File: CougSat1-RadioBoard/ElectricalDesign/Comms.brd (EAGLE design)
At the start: 90.4 x 95.8 mm, 409 parts, among them J1 700mm Antenna, J2 CougSat Card, J3 230mm Antenna, J4 SWD, Q1 DMN53D0LDW, Q2 DMN53D0LDW, Q3 DMN53D0LDW, Q4 CSD25402Q3A, Q5 CSD25402Q3A, U1 AD8515, U10 AD8515, U11 AD8515, U12 TXS0102DQM, U13 ADF4360, U14 MAAM-011229, U15 INA199C2, U16 AD8515, U17 AD8515, U18 LP5907MFX-3.1, U19 HMC545A, U2 AD8515, U20 INA199C1, U21 TPS61236, U22 AD8345, U23 AD9761, U24 TXS0102DQM, U25 TXS0102DQM, U26 TXS0102DQM, U27 MMZ09332B, U28 AD8515, U29 ADF4360, U3 AD7291, U30 TXS0102DQM, U31 INA199C2, U32 TXS0102DQM, U33 LP5907MFX-3.1, U34 MAAM-011229, U35 TXS0102DQM, U36 TXS0102DQM, U37 AD9761, U38 AD8346, U39 TXS0102DQM, U4 AD7291, U40 STM32L496VGT, U41 HMC452QS16G, U42 TXS0102DQM, U43 INA199C2, U44 ADF4360, U45 LP5907MFX-3.1, U46 IS25LP016D, U47 IS25LP016D, U48 GRF2133, U49 INA199C1, U5 MAAM-011229, U6 AD8348, U7 AD7291, U8 MAAM-011229, U9 TXS0102DQM, Y1 19.68MHz ±2.5ppm, Y2 19.68MHz ±2.5ppm, Y3 8MHz ±10ppm, Y4 32.768kHz ±10ppm, Y5 19.68MHz ±2.5ppm

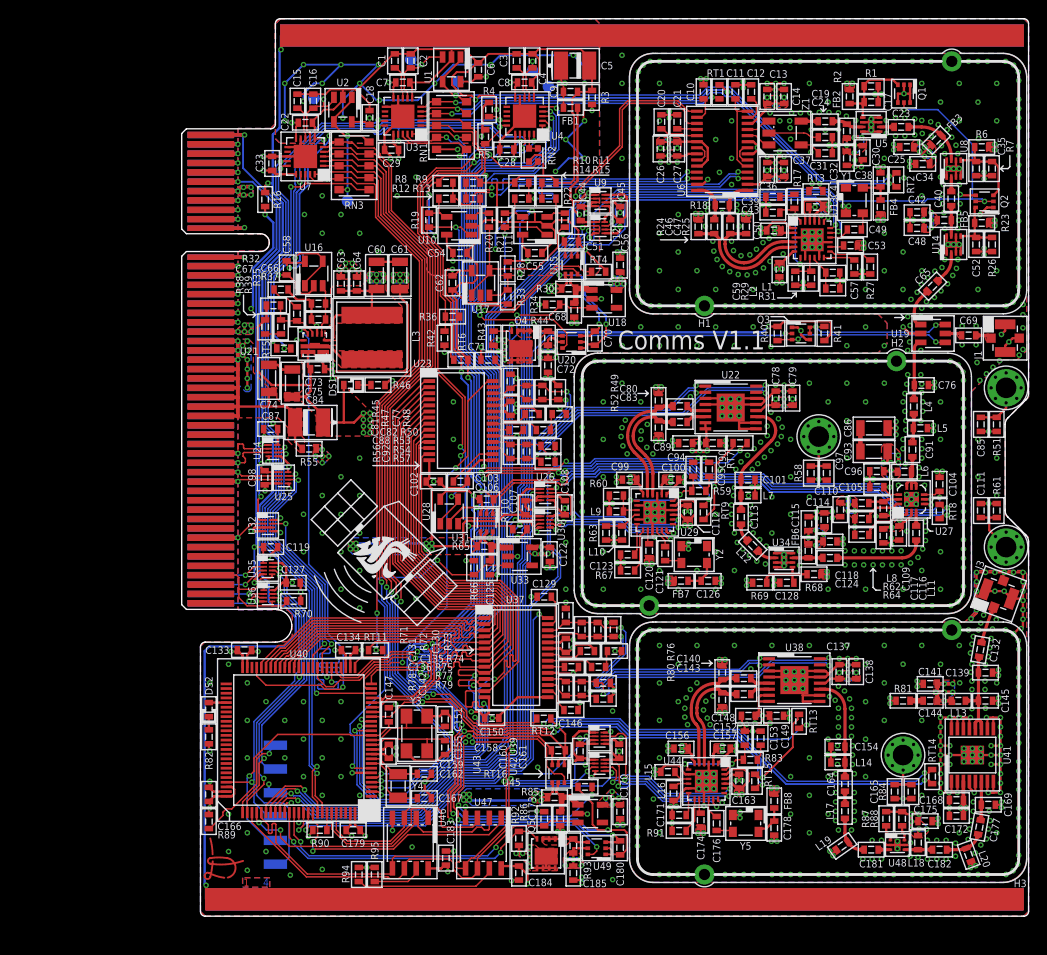
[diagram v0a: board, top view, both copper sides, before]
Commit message: Removed 230mm circuits
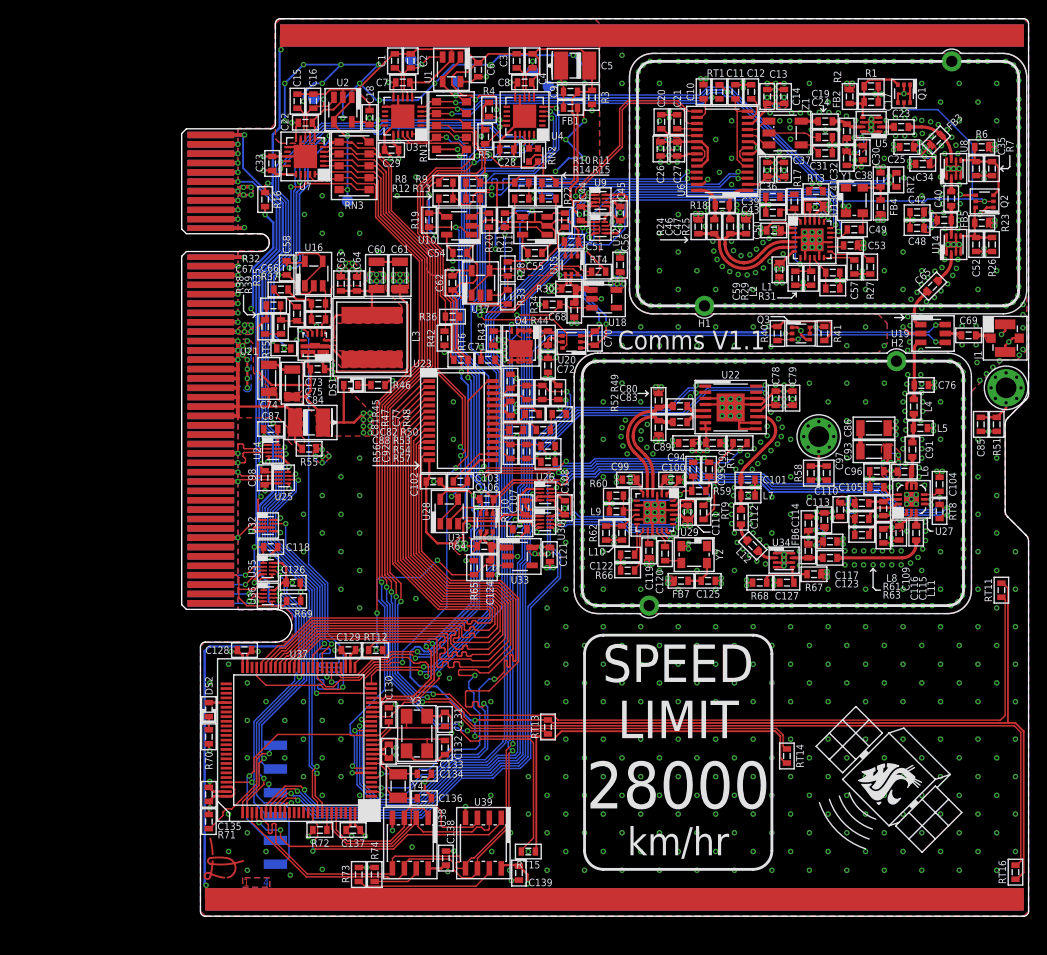
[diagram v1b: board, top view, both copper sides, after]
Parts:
- removed C140, C143, C176: 1nF 1%, CougsInSpace-Capacitors:1608
- removed C141, C170, C172, C173, C174, C185: 1µF 10%, CougsInSpace-Capacitors:1608
- removed C142: 560pF 1%, CougsInSpace-Capacitors:1608
- removed C144, C149, C168: 100pF 1%, CougsInSpace-Capacitors:1608
- removed C145: 2pF ±0.1pF, CougsInSpace-Capacitors:1608
- removed C146, C147, C150, C156, C157, C158, C159, C160, C161, C163, C165, C166, C175, C178, C179, C180, C183, C184: 100nF 10%, CougsInSpace-Capacitors:1608
- removed C148, C171: 10nF 10%, CougsInSpace-Capacitors:1608
- removed C151, C155: 8pF ±0.25, CougsInSpace-Capacitors:1608
- removed C152: 56pF 2%, CougsInSpace-Capacitors:1608
- removed C153: 270pF 1%, CougsInSpace-Capacitors:1608
- removed C154, C177: 10pF 5%, CougsInSpace-Capacitors:1608
- removed C162, C167: 15pF 1%, CougsInSpace-Capacitors:1608
- removed C164: 0.8pF ±0.1pF, CougsInSpace-Capacitors:1608
- removed C169: 4.7pF ±0.1, CougsInSpace-Capacitors:1608
- removed C181, C182: 33pF 5%, CougsInSpace-Capacitors:1608
- removed FB8: 1.5kΩ @ 100MHz, CougsInSpace-Coils:1608
- removed H5, H6, H7: M2, CougsInSpace-Hardware:MOUNTING_HOLE-2.2
- removed J4: SWD, CougsInSpace-Connectors:SMD2.54-1X06-R
- removed L13, L17, L20: 22nH 2%, CougsInSpace-Coils:1608
- removed L14, L15, L16: 1.6nH 5%, CougsInSpace-Coils:1608
- removed L18: 33nH 2%, CougsInSpace-Coils:1608
- removed L19: 18nH 2%, CougsInSpace-Coils:1608
- removed Q5: CSD25402Q3A, CougsInSpace-DiscreteSemi:SON-3333
- removed R75, R82, R89: 1kΩ 0.1%, CougsInSpace-Resistors:1608
- removed R76, R80: 49.9Ω 0.1%, CougsInSpace-Resistors:1608
- removed R77, R79: 1.33kΩ 0.1%, CougsInSpace-Resistors:1608
- removed R78: 1.74kΩ 0.1%, CougsInSpace-Resistors:1608
- removed R81: 5.6Ω 1%, CougsInSpace-Resistors:1608
- removed R83: 102kΩ 0.1%, CougsInSpace-Resistors:1608
- removed R84, R90: 0Ω <20mΩ, CougsInSpace-Resistors:1608
- removed R85, R93: 50mΩ 1%, CougsInSpace-Resistors:1608
- removed R86, R92, R94, R95: 10kΩ 0.1%, CougsInSpace-Resistors:1608
- removed R87, R91: 4.7kΩ 0.1%, CougsInSpace-Resistors:1608
- removed R88: 75Ω 0.1%, CougsInSpace-Resistors:1608
- removed U40: STM32L496VGT, CougsInSpace-IC-µController:QFP-100-1414
- removed U41: HMC452QS16G, CougsInSpace-RF:QSOP-16
- removed U42: TXS0102DQM, CougsInSpace-IC-Comms:X2SON-8
- removed U43: INA199C2, CougsInSpace-IC-Amplifiers:SOT363
- removed U44: ADF4360, CougsInSpace-RF:QFN-24-4040
- removed U45: LP5907MFX-3.1, CougsInSpace-IC-Power:SOT23-5
- removed U46, U47: IS25LP016D, CougsInSpace-IC-Memory:SO8
- removed U48: GRF2133, CougsInSpace-RF:DFN-6-1515
- removed U49: INA199C1, CougsInSpace-IC-Amplifiers:SOT363
- removed Y5: 19.68MHz ±2.5ppm, CougsInSpace-Clocks:SMD-3225
- C112: value 100nF 10% -> 2.4pF ±0.1pF
- C113: value 2.4pF ±0.1pF -> 100nF 10%
- C114: value 100nF 10% -> 47pF 5%
- C115: value 47pF 5% -> 100pF 1%
- C116: value 100pF 1% -> 1µF 10%
- C117, C120: value 1µF 10% -> 1nF 1%
- C118, C128: value 1nF 1% -> 100nF 10%
- C119: value 100nF 10% -> 1µF 10%
- C121, C124: value 1nF 1% -> 1µF 10%
- C122: value 1µF 10% -> 10nF 10%
- C123: value 10nF 10% -> 1nF 1%
- C125: value 1µF 10% -> 100nF 10%
- C127: value 100nF 10% -> 1nF 1%
- C130: value 560pF 1% -> 100nF 10%
- C131: value 100nF 10% -> 8pF ±0.25
- C132: value 100pF 1% -> 8pF ±0.25
- C134, C136: value 100nF 10% -> 15pF 1%
- C137: value 100pF 1% -> 100nF 10%
- C138: value 10nF 10% -> 100nF 10%
- C139: value 4.7pF ±0.1 -> 100nF 10%
- H3: value Can - 230mm -> M2; device CougsInSpace-Hardware:SHIELD-2641 -> CougsInSpace-Hardware:MOUNTING_HOLE-2.2
- J3: value 230mm Antenna -> SWD; device CougsInSpace-Connectors:U.FL -> CougsInSpace-Connectors:SMD2.54-1X06-R
- LOGO1: value SIGNATUREBRADLEY -> Satellite 16mm; device CougsInSpace-Aesthetics:SIGN-BRADLEY -> CougsInSpace-Aesthetics:CIS-SATELLITE-16
- LOGO2: value Satellite 16mm -> SIGNATUREBRADLEY; device CougsInSpace-Aesthetics:CIS-SATELLITE-16 -> CougsInSpace-Aesthetics:SIGN-BRADLEY
- R61: value 0Ω <20mΩ -> 2kΩ 0.1%
- R62: value 2kΩ 0.1% -> 470Ω 0.5%
- R63: value 470Ω 0.5% -> 1.74kΩ 0.1%
- R64: value 1.74kΩ 0.1% -> 50mΩ 1%
- R65: value 50mΩ 1% -> 10kΩ 0.1%
- R66: value 10kΩ 0.1% -> 4.7kΩ 0.1%
- R67: value 4.7kΩ 0.1% -> 2kΩ 0.1%
- R69: value 2kΩ 0.1% -> 1kΩ 0.1%
- R71: value 1.33kΩ 0.1% -> 1kΩ 0.1%
- R72: value 1.74kΩ 0.1% -> 0Ω <20mΩ
- R73: value 1.33kΩ 0.1% -> 10kΩ 0.1%
- R74: value 8.45kΩ 0.1% -> 10kΩ 0.1%
- U37: value AD9761 -> STM32L496VGT; device CougsInSpace-IC-Conversion:SSOP-28 -> CougsInSpace-IC-µController:QFP-100-1414
- U38: value AD8346 -> IS25LP016D; device CougsInSpace-RF:TSSOP-16 -> CougsInSpace-IC-Memory:SO8
- U39: value TXS0102DQM -> IS25LP016D; device CougsInSpace-IC-Comms:X2SON-8 -> CougsInSpace-IC-Memory:SO8
- moved J3 75.6 mm to (15.0, -36.0), flipped to the bottom, turned to 90 degrees
- moved LOGO1 71.5 mm to (75.5, -33.3)
- moved RT11 67.1 mm to (87.5, -13.1), turned to 90 degrees
- moved C118 59.7 mm to (9.50, -8.50)
- moved C128 58.3 mm to (6.70, -19.5), turned to 0 degrees
- moved C132 58.1 mm to (28.1, -29.9), turned to 270 degrees
- moved C137 54.6 mm to (18.3, -38.7), turned to 180 degrees
- moved C139 54.2 mm to (36.0, -43.3), turned to 270 degrees
- moved C127 52.7 mm to (64.6, -12.3), turned to 180 degrees
- moved R69 49.8 mm to (11.9, -14.2), turned to 180 degrees
- moved LOGO3 48.7 mm to (53.0, -29.9), flipped to the top
- moved C138 48.1 mm to (28.2, -41.7)
- moved RT16 46.8 mm to (89.0, -43.2), turned to 270 degrees
- moved U38 44.5 mm to (24.4, -40.1), turned to 270 degrees
- moved C126 44.3 mm to (11.9, -12.3)
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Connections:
- removed net !230_CS: U39.7, U44.19
- removed net !PC_5.0V-0: Q5.4, R92.1, U40.86
- removed net !RFCLK_CS-230: U39.2, U40.89
- removed net 230_MOSI: U42.6, U44.18
- removed net 230_SCK: U42.7, U44.17
- removed net 3.1V_0: C131.1, C135.1, C137.1, C138.1, C148.1, C149.1, C156.1, C157.1, C161.1, C163.1, C170.1, C174.1, FB8.2, R76.2, R80.2, U37.23, U38.12, U38.7, U38.8, U39.5, U39.8, U42.5, U42.8, U44.2, U44.21, U44.23, U44.6, U45.5
- removed net 5.0V_0: C141.1, C144.1, C168.1, C172.1, C175.1, C185.1, L13.2, L18.2, R87.2, R88.2, R93.1, U41.3, U49.5
- removed net ANTENNA_230_COAX: C132.2, J3.CENTER
- removed net CHASSIS_230-0: C111.1, H5.1, H5.V1, H5.V2, H5.V3, H5.V4, H5.V5, H5.V6, H5.V7, H5.V8, R61.2
- removed net CHASSIS_230-1: C165.1, H4.1, H4.V1, H4.V2, H4.V3, H4.V4, H4.V5, H4.V6, H4.V7, H4.V8, R84.2
- removed net DAC_BUS_CLK-230: U37.11, U37.12, U40.4
- removed net DAC_COMP1-230: C129.1, U37.27
- removed net DAC_COMP2-230: C135.2, U37.22
- removed net DAC_COMP3-230: C146.1, U37.16
- removed net DAC_FSADJ-230: R75.2, U37.21
- removed net DAC_FSASJ_MID-230: R74.2, R75.1
- removed net DAC_REFIO-230: C136.1, U37.20
- removed net DAC_SLEEP-230: U37.28, U40.88
- removed net I_3.1V-0: U4.2, U43.6
- removed net I_3.1V-0N: C173.1, R85.1, U43.5, U45.1
- removed net I_5.0V-0: U4.1, U49.6
- removed net I_5.0V-0P: Q5.1, Q5.2, Q5.3, R93.2, U49.4
- removed net MOD_230_ID_N: C130.2, R72.1, R73.2, U37.25, U38.2
- removed net MOD_230_ID_P: C130.1, R71.2, R72.2, U37.26, U38.1
- removed net MOD_230_LOI_N: C140.2, U38.5
- removed net MOD_230_LOI_P: C143.2, U38.6
- removed net MOD_230_QD_N: C142.2, R77.2, R78.1, U37.18, U38.15
- removed net MOD_230_QD_P: C142.1, R78.2, R79.2, U37.17, U38.16
- removed net MOD_230_RFOUT: C154.1, C164.1, L14.2, U38.11
- removed net MOD_LNA_230_EN: R87.1, U48.1
- removed net MOD_LNA_230_RFIN: C181.2, U48.3
- removed net MOD_LNA_230_RFINMID1: C164.2, L17.1
- removed net MOD_LNA_230_RFINMID2: C181.1, L17.2, L19.2
- removed net MOD_LNA_230_RFOUT: C182.1, L18.1, U48.4
- removed net MOD_LNA_230_VDD1: R88.1, U48.6
- removed net MOD_PA_230_RC: C144.2, R81.2
- removed net MOD_PA_230_RFIN: C169.1, C177.2, U41.6
- removed net MOD_PA_230_RFINMID: C177.1, C182.2, L20.2
- removed net MOD_PA_230_RFOUT: C132.1, C139.1, C145.1, L13.1, U41.11, U41.12
- removed net MUXOUT-230: U40.90, U44.20
- removed net PC_3.1V-0: R86.2, U40.87, U45.3
- removed net REF_CLK_VDD-0: C178.1, FB8.1, Y5.4
- removed net RFCLK_CC-230: C171.1, U44.12
- removed net RFCLK_CN-230: C174.2, U44.14
- removed net RFCLK_CP-230: C152.1, R83.2, U44.24, U44.7
- removed net RFCLK_L1-230: L15.2, U44.9
- removed net RFCLK_L2-230: L16.2, U44.10
- removed net RFCLK_OUT-230_N: C140.1, R76.1, U44.5
- removed net RFCLK_OUT-230_P: C143.1, R80.1, U44.4
- removed net RFCLK_REFIN-230: C176.2, U44.16
- removed net RFCLK_REFOUT-230: C176.1, Y5.3
- removed net RFCLK_RSET-230: R91.2, U44.13
- removed net RFCLK_VTUNE_FILTER-230: C153.1, R83.1
- removed net TEMP_CLK_230: RN3.8, RT15.1, U7.2
- removed net TEMP_DAC_230: RN3.7, RT12.1, U7.20
- removed net TEMP_LDO-0: RN3.3, RT16.1, U7.1
- removed net TEMP_MOD_230: RN3.9, RT13.1, U7.4
- removed net TEMP_PA_230: RN3.2, RT14.1, U7.3
- new net TEMP_PCB_0: RN3.7, RT13.1, U7.20
- new net TEMP_PCB_1: RN3.3, RT15.1, U7.1
- new net TEMP_PCB_2: RN3.8, RT14.1, U7.2
- new net TEMP_PCB_3: RN3.2, RT16.1, U7.3
- new net TEMP_PCB_4: RN3.9, RT11.1, U7.4
- net !ADC_RESET: now also U37.29; no longer U40.29
- net !COM_SPI_CS: now also U37.35; no longer U40.35
- net !FLASH_CS-A: now also U37.91, U39.1; no longer U40.91, U47.1
- net !FLASH_CS-B: now also U37.95, U38.1; no longer U40.95, U46.1
- net !FLASH_WP: now also U37.96, U38.3, U39.3; no longer U40.96, U46.3, U47.3
- net !NRST: now also C130.1, J3.5, U37.14; no longer C147.1, J4.5, U40.14
- net !PC_5.0V-1: now also U37.17; no longer U40.17
- net !RFCLK_CS-DEMOD: now also U37.18; no longer U40.18
- net !RFCLK_CS-MOD: now also U37.83; no longer U40.83
- net !RX_LNA_EN: now also U37.15; no longer U40.15
- net 3.1V_1: now also C111.1, C113.1, C117.1, C119.1, C121.1, R67.2; no longer C112.1, C115.1, C118.1, C120.1, C122.1, R68.2
- net 3.3V_5: now also C118.1; no longer C119.1
- net 3.3V_6: now also C126.1, C128.1, C129.1, C135.1, C137.1, C138.1, C139.1, R64.2, R71.2, R73.2, R74.2, U37.100, U37.11, U37.28, U37.50, U37.6, U37.73, U37.75, U38.8, U39.8; no longer C127.1, C134.1, C150.1, C159.1, C160.1, C166.1, C179.1, C183.1, C184.1, R65.2, R85.2, R89.2, R94.2, R95.2, U37.14, U39.1, U40.100, U40.11, U40.28, U40.50, U40.6, U40.73, U40.75, U42.1, U43.4, U46.8, U47.8
- net 5.0V: no longer Q5.5, Q5.6, Q5.7, Q5.8, Q5.PAD, R92.2
- net 5.0V_1: now also C115.1, R61.2, R63.2; no longer C117.1, R62.2, R64.2
- net AGND: now also U37.19, U37.20; no longer C158.2, C180.2, U40.19, U40.20, U43.1, U43.2, U49.1, U49.2
- net ANTENNA_SW: now also U37.82; no longer U40.82
- net AVDD: now also U37.21, U37.22; no longer C158.1, C180.1, U40.21, U40.22, U43.3, U49.3
- net BOOT0: now also R72.2, U37.94; no longer R90.2, U40.94
- net CHASSIS_700-0: now also H4.1, H4.V1, H4.V2, H4.V3, H4.V4, H4.V5, H4.V6, H4.V7, H4.V8; no longer H7.1, H7.V1, H7.V2, H7.V3, H7.V4, H7.V5, H7.V6, H7.V7, H7.V8
- net CHASSIS_700-1: now also H3.1, H3.V1, H3.V2, H3.V3, H3.V4, H3.V5, H3.V6, H3.V7, H3.V8; no longer H6.1, H6.V1, H6.V2, H6.V3, H6.V4, H6.V5, H6.V6, H6.V7, H6.V8
- net COM_SPI_MISO: now also U37.31; no longer U40.31
- net COM_SPI_MOSI: now also U37.32; no longer U40.32
- net COM_SPI_SCK: now also U37.23; no longer U40.23
- net CTRL_SYNC: now also U37.33; no longer U40.33
- net DAC_BUS_0: now also U37.5; no longer U37.10, U40.5
- net DAC_BUS_1: now also U37.38; no longer U37.9, U40.38
- net DAC_BUS_2: now also U37.39; no longer U37.8, U40.39
- net DAC_BUS_3: now also U37.40; no longer U37.7, U40.40
- net DAC_BUS_4: now also U37.41; no longer U37.6, U40.41
- net DAC_BUS_5: now also U37.42; no longer U37.5, U40.42
- net DAC_BUS_6: now also U37.43; no longer U37.4, U40.43
- net DAC_BUS_7: now also U37.44; no longer U37.3, U40.44
- net DAC_BUS_8: now also U37.45; no longer U37.2, U40.45
- net DAC_BUS_9: now also U37.46; no longer U37.1, U40.46
- net DAC_BUS_CLK-700: now also U37.3; no longer U40.3
- net DAC_SELECT_I/!Q: now also U37.2; no longer U37.13, U40.2
- net DAC_SLEEP-700: now also U37.34; no longer U40.34
- net DEMOD_ENABLE: now also U37.25; no longer U40.25
- net DEMOD_ID: now also U37.24; no longer U40.24
- net DEMOD_QD: now also U37.26; no longer U40.26
- net DEMOD_VGIN: now also U37.30; no longer U40.30
- net DGND: now also C113.2, C121.2, C124.2, C130.2, C132.2, C135.2, J3.3, R62.1, R65.1, R68.1, R72.1, U37.10, U37.27, U37.49, U37.74, U37.99; no longer C112.2, C119.2, C123.2, C141.2, C145.2, C146.2, C147.2, C148.2, C149.2, C150.2, C151.2, C152.2, C153.2, C154.2, C155.2, C156.2, C157.2, C159.2, C160.2, C161.2, C162.2, C163.2, C165.2, C166.2, C167.2, C168.2, C169.2, C170.2, C171.2, C172.2, C173.2, C175.2, C178.2, C179.2, C183.2, C184.2, C185.2, H3.1, H3.2, J3.SHIELD@1, J3.SHIELD@13, J3.SHIELD@2, J4.3, L14.1, L15.1, L16.1, L19.1, L20.1, R61.1, R63.1, R67.1, R71.1, R73.1, R74.1, R77.1, R79.1, R81.1, R82.1, R84.1, R86.1, R90.1, R91.1, U37.15, U37.19, U37.24, U38.10, U38.13, U38.14, U38.3, U38.9, U38.PAD, U39.3, U39.6, U40.10, U40.27, U40.49, U40.74, U40.99, U41.1, U41.10, U41.13, U41.14, U41.15, U41.16, U41.2, U41.4, U41.5, U41.7, U41.8, U41.9, U41.PAD, U42.4, U44.1, U44.11, U44.15, U44.22, U44.3, U44.8, U44.PAD, U45.2, U46.4, U47.4, U48.2, U48.5, U48.PAD, Y5.2
- net FLASH_HOLD-A: now also R73.1, U39.7; no longer R94.1, U47.7
- net FLASH_HOLD-B: now also R74.1, U38.7; no longer R95.1, U46.7
- net I2C_SCL: now also U37.92; no longer U40.92
- net I2C_SDA: now also U37.93; no longer U40.93
- net I_3.1V-1N: now also C124.1, R64.1; no longer C125.1, R65.1
- net JTAG_EN_COMMS: now also R69.2; no longer R70.2
- net JTAG_TCK: now also J3.2, U37.76; no longer J4.2, U40.76
- net JTAG_TDI: now also U37.77; no longer U40.77
- net JTAG_TDO: now also J3.6, U37.37; no longer J4.6, U40.37
- net JTAG_TMS: now also J3.4, U37.72; no longer J4.4, U40.72
- net LED_A: now also U37.55; no longer U40.55
- net LED_C: now also R70.2; no longer R82.2
- net MOD_700_RFOUT: now also C112.1; no longer C113.1
- net MOD_LNA_700_RFINMID: now also C112.2; no longer C113.2
- net MOD_LNA_700_RFOUT: now also C123.1; no longer C124.1
- net MOD_PA_700_RFINMID: now also C123.2; no longer C124.2
- net MUXOUT-DEMOD: now also U37.81; no longer U40.81
- net MUXOUT-MOD: now also U37.85; no longer U40.85
- net OSC32_IN: now also C136.1, U37.8; no longer C167.1, U40.8
- net OSC32_OUT: now also C134.1, U37.9; no longer C162.1, U40.9
- net OSC_IN: now also C132.1, U37.12; no longer C155.1, U40.12
- net OSC_OUT: now also C131.1, U37.13; no longer C151.1, U40.13
- net PA_PD-700: now also U37.84; no longer U40.84
- net PA_VBA1-700: now also R63.1; no longer R64.1
- net PA_VBA2-700: now also R61.1; no longer R62.1
- net PC_3.1V-1: now also R65.2, U37.7; no longer R66.2, U40.7
- net PC_3.1V-2: now also U37.16; no longer U40.16
- net PREAMP_700_BIAS: now also C127.1, R67.1, R68.2; no longer C128.1, R68.1, R69.2
- net REF_CLK_VDD-1: now also C125.1; no longer C126.1
- net REG_EN-5: now also U37.47; no longer U40.47
- net RFCLK_CC-MOD: now also C122.1; no longer C123.1
- net RFCLK_CN-MOD: now also C119.2; no longer C120.2
- net RFCLK_L2-MOD: now also R62.2; no longer R63.2
- net RFCLK_REFIN-MOD: now also C120.2; no longer C121.2
- net RFCLK_REFOUT-MOD: now also C120.1; no longer C121.1
- net RFCLK_RSET-MOD: now also R66.2; no longer R67.2
- net SPI_MISO: now also U37.79, U38.2, U39.2; no longer U40.79, U46.2, U47.2
- net SPI_MOSI: now also U37.80, U38.5, U39.5; no longer U40.80, U42.3, U46.5, U47.5
- net SPI_SCK: now also U37.78, U38.6, U39.6; no longer U40.78, U42.2, U46.6, U47.6
- net SWD_VSENSE: now also J3.1, R71.1; no longer J4.1, R89.1
- net TEMP_COMMS: now also RT12.1; no longer RT11.1
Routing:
- net TEMP_PCB_3: track 0.00 -> 149.6 mm, vias 0 -> 2
- net TEMP_PCB_4: track 0.00 -> 146.4 mm, vias 0 -> 2
- net TEMP_PA_230: track 129.1 -> 0.00 mm, vias 4 -> 0
- net 3.1V_0: track 127.6 -> 0.00 mm, vias 31 -> 0
- net TEMP_MOD_230: track 115.5 -> 0.00 mm, vias 4 -> 0
- net TEMP_CLK_230: track 112.2 -> 0.00 mm, vias 4 -> 0
- net TEMP_PCB_2: track 0.00 -> 111.0 mm, vias 0 -> 2
- net I_5.0V-0: track 108.5 -> 0.00 mm, vias 4 -> 0
- net TEMP_LDO-0: track 98.8 -> 0.00 mm, vias 4 -> 0
- net I_3.1V-0: track 95.9 -> 0.00 mm, vias 2 -> 0
- net TEMP_PCB_1: track 0.00 -> 95.1 mm, vias 0 -> 2
- net TEMP_DAC_230: track 87.5 -> 0.00 mm, vias 2 -> 0
- net 5.0V_0: track 86.0 -> 0.00 mm, vias 19 -> 0
- net TEMP_PCB_0: track 0.00 -> 84.1 mm, vias 0 -> 2
- net 3.3V_6: track 426.6 -> 350.6 mm, vias 48 -> 34
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- removed copper zone on layer 1, net 3.1V_0
- removed copper zone on layer 15, net 3.1V_0
- removed copper zone on layer 16, net 3.1V_0
- removed copper zone on layer 2, net 3.1V_0
- removed copper zone on layer 1, net 5.0V_0
- removed copper zone on layer 15, net 5.0V_0
- removed copper zone on layer 16, net 5.0V_0
- removed copper zone on layer 2, net 5.0V_0
- removed copper zone on layer 1, net ANTENNA_230_COAX
- removed copper zone on layer 15, net CHASSIS_230-0
- removed copper zone on layer 2, net CHASSIS_230-0
- removed copper zone on layer 15, net CHASSIS_230-1
- removed copper zone on layer 2, net CHASSIS_230-1
- removed copper zone on layer 1, net I_5.0V_P
- removed copper zone on layer 1, net MOD_230_RFOUT
- removed copper zone on layer 1, net MOD_LNA_230_RFIN
- removed copper zone on layer 1, net MOD_LNA_230_RFINMID1
- removed copper zone on layer 1, net MOD_LNA_230_RFINMID2
- removed copper zone on layer 1, net MOD_LNA_230_RFOUT
- removed copper zone on layer 1, net MOD_PA_230_RFIN
- removed copper zone on layer 1, net MOD_PA_230_RFINMID
- removed copper zone on layer 1, net MOD_PA_230_RFOUT
- removed copper zone on layer 1, net RFCLK_OUT-230_N
- removed copper zone on layer 1, net RFCLK_OUT-230_P

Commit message: Updated off-sheet connectors
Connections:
- net DAC_BUS_CLK-700 renamed DAC_BUS_CLK
- net PA_PD-700 renamed PA_PD
- net DGND: now also U4.1, U4.2
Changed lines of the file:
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@@
 <wire x1="33" y1="-25" x2="37" y2="-25" width="0.25" layer="2"/>
 <wire x1="37" y1="-25" x2="39" y2="-23" width="0.25" layer="2"/>
+<contactref element="U4" pad="2"/>
+<contactref element="U4" pad="1"/>
+<wire x1="38.5" y1="36.5" x2="38.5" y2="37" width="0" layer="19" extent="1-1"/>
+<wire x1="36.6" y1="37.5" x2="38.5" y2="37" width="0" layer="19" extent="1-1"/>
 </signal>
 <signal name="AGND" class="4">
@@
 <wire x1="30.4" y1="-23.85" x2="32.82" y2="-23.85" width="0.16" layer="1"/>
 </signal>
-<signal name="DAC_BUS_CLK-700">
+<signal name="DAC_BUS_CLK">
 <contactref element="U37" pad="3"/>
 <contactref element="U23" pad="12"/>
@@
 <wire x1="72.45" y1="1.7" x2="72.45" y2="4.2" width="0.5" layer="1"/>
 </signal>
-<signal name="PA_PD-700">
+<signal name="PA_PD">
 <contactref element="U27" pad="10"/>
 <contactref element="C105" pad="1"/>

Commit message: Re-exported gerbers with minor corrections
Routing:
- net DGND: track 2440.9 -> 2443.5 mm
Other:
- board text added: "Comms V1.2"
- board text removed: "Comms V1.1"
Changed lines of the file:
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@@
 <wire x1="77.1" y1="16" x2="76.8" y2="16.3" width="0.15" layer="21"/>
 <wire x1="77.1" y1="16" x2="76.8" y2="15.7" width="0.15" layer="21"/>
-<text x="54.4" y="13.6" size="2" layer="21" font="vector" ratio="15" align="center">Comms V1.1</text>
+<text x="54.4" y="13.6" size="2" layer="21" font="vector" ratio="15" align="center">Comms V1.2</text>
 <text x="6.9" y="-44.3" size="0.8" layer="1" font="vector" ratio="15" align="center">1</text>
 <text x="7.6" y="-44.3" size="0.8" layer="2" font="vector" ratio="15" align="center">2</text>
@@
 <contactref element="U4" pad="2"/>
 <contactref element="U4" pad="1"/>
-<wire x1="38.5" y1="36.5" x2="38.5" y2="37" width="0" layer="19" extent="1-1"/>
-<wire x1="36.6" y1="37.5" x2="38.5" y2="37" width="0" layer="19" extent="1-1"/>
+<wire x1="38.5" y1="36.5" x2="38.5" y2="37" width="0.25" layer="1"/>
+<wire x1="38.5" y1="37" x2="37.1" y2="37" width="0.25" layer="1"/>
+<wire x1="37.1" y1="37" x2="36.6" y2="37.5" width="0.25" layer="1"/>
 </signal>
 <signal name="AGND" class="4">
@@
 <wire x1="30.055" y1="-6.01" x2="30.055" y2="-7.855" width="0.25" layer="1"/>
 <wire x1="30.055" y1="-7.855" x2="30.3" y2="-8.1" width="0.25" layer="1"/>
-<wire x1="11.45" y1="-2.25" x2="26.1" y2="-1.5" width="0" layer="19" extent="1-1"/>
 </signal>
 <signal name="FLASH_HOLD-A">

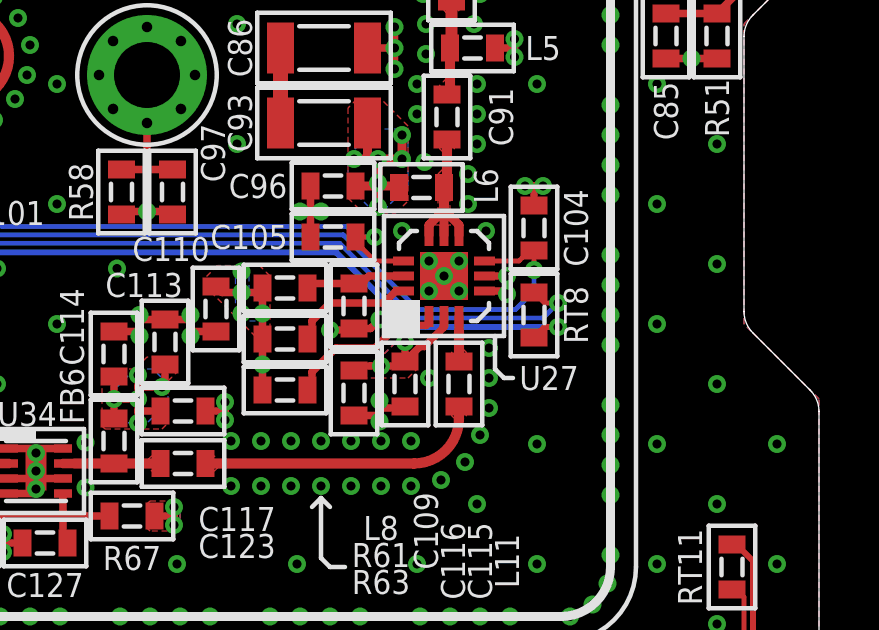
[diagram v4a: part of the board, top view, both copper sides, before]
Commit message: added heatsink traces
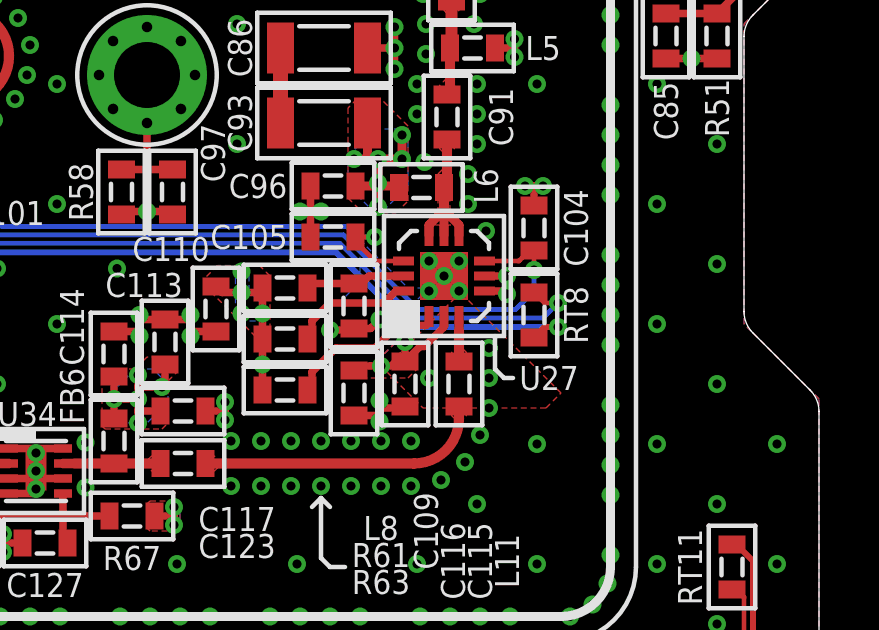
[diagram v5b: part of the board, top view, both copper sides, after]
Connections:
- new net SELFNET: U27.PAD
- net DGND: no longer U27.PAD
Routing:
- net DGND: track 2443.5 -> 2435.8 mm, vias 950 -> 949
- added copper zone on layer 16, net HEAT1
- added copper zone on layer 15, net HEAT2
- added copper zone on layer 2, net HEAT3
- added copper zone on layer 1, net HEAT4
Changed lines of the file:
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@@
 <contactref element="U27" pad="4"/>
 <contactref element="U27" pad="5"/>
-<contactref element="U27" pad="PAD"/>
 <wire x1="79.25" y1="-3.4" x2="80" y2="-3.4" width="0.25" layer="1"/>
 <wire x1="79.25" y1="-3.9" x2="79.9" y2="-3.9" width="0.25" layer="1"/>
 <wire x1="79.9" y1="-3.9" x2="80" y2="-4" width="0.25" layer="1"/>
 <wire x1="80" y1="-3.4" x2="80" y2="-4" width="0.25" layer="1"/>
-<wire x1="77.9" y1="-3.4" x2="78.4" y2="-3.9" width="0.25" layer="1"/>
-<wire x1="77.9" y1="-3.4" x2="77.4" y2="-3.9" width="0.25" layer="1"/>
-<wire x1="77.9" y1="-3.4" x2="77.4" y2="-2.9" width="0.25" layer="1"/>
-<wire x1="77.9" y1="-3.4" x2="78.4" y2="-2.9" width="0.25" layer="1"/>
 <wire x1="75.35" y1="4.2" x2="76.25" y2="4.2" width="0.25" layer="1"/>
 <wire x1="76.25" y1="4.2" x2="76.25" y2="4.9" width="0.25" layer="1"/>
@@
 <via x="78.7" y="0" extent="1-16" drill="0.3"/>
 <via x="77.25" y="0.4" extent="1-16" drill="0.3"/>
-<via x="76.5" y="-1.9" extent="1-16" drill="0.3"/>
 <via x="79.3" y="-1.9" extent="1-16" drill="0.3"/>
 <via x="79" y="2" extent="1-16" drill="0.3"/>
@@
 <wire x1="71" y1="1" x2="73.1" y2="-1.1" width="0.25" layer="2"/>
 <wire x1="73.1" y1="-1.1" x2="73.1" y2="-1.25" width="0.25" layer="2"/>
-<wire x1="76.5" y1="-1.9" x2="77.4" y2="-2.8" width="0.25" layer="2"/>
-<wire x1="77.4" y1="-2.8" x2="77.4" y2="-2.9" width="0.25" layer="2"/>
-<wire x1="78.4" y1="-3.9" x2="79.4" y2="-4.9" width="0.25" layer="2"/>
-<wire x1="79.4" y1="-4.9" x2="79.4" y2="-5.8" width="0.25" layer="2"/>
-<wire x1="78.4" y1="-2.9" x2="79.3" y2="-2" width="0.25" layer="2"/>
 <wire x1="79.3" y1="-2" x2="79.3" y2="-1.9" width="0.25" layer="2"/>
 <wire x1="80" y1="-3.4" x2="80" y2="-2.6" width="0.25" layer="2"/>
@@
 <wire x1="87.4" y1="-26.975" x2="40.175" y2="-26.975" width="0.16" layer="1"/>
 </signal>
+<signal name="SELFNET">
+<contactref element="U27" pad="PAD"/>
+</signal>
+<signal name="HEAT1">
+<polygon width="0.1524" layer="16">
+<vertex x="77.4" y="-3.8"/>
+<vertex x="76.9" y="-4.3"/>
+<vertex x="74.4" y="-4.3"/>
+<vertex x="75.1" y="-3.6"/>
+<vertex x="75.1" y="-2.2"/>
+<vertex x="76.7" y="-3.8"/>
+</polygon>
+</signal>
+<signal name="HEAT2">
+<polygon width="0.1524" layer="15">
+<vertex x="77.3" y="-2.9"/>
+<vertex x="74.5" y="-2.9"/>
+<vertex x="74.4" y="-3"/>
+<vertex x="74.4" y="-1.1"/>
+<vertex x="75.5" y="0"/>
+<vertex x="76.7" y="0"/>
+<vertex x="77.3" y="-0.6"/>
+</polygon>
+</signal>
+<signal name="HEAT4">
+<polygon width="0.1524" layer="1">
+<vertex x="78.5" y="-3.9"/>
+<vertex x="76" y="-6.4"/>
+<vertex x="76" y="-6.6"/>
+<vertex x="77.2" y="-7.8"/>
+<vertex x="79.5" y="-7.8"/>
+<vertex x="81.3" y="-7.8"/>
+<vertex x="81.8" y="-7.3"/>
+<vertex x="78.5" y="-4"/>
+</polygon>
+</signal>
+<signal name="HEAT3">
+<polygon width="0.1524" layer="2">
+<vertex x="78.4" y="-2.9"/>
+<vertex x="76.9" y="-1.4"/>
+<vertex x="76.2" y="-1.4"/>
+<vertex x="77.7" y="0.1"/>
+<vertex x="78" y="0.1"/>
+<vertex x="79.6" y="-1.5"/>
+<vertex x="79.6" y="-2.9"/>
+</polygon>
+</signal>
 </signals>
